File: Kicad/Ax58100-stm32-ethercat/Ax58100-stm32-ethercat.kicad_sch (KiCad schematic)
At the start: 0 parts

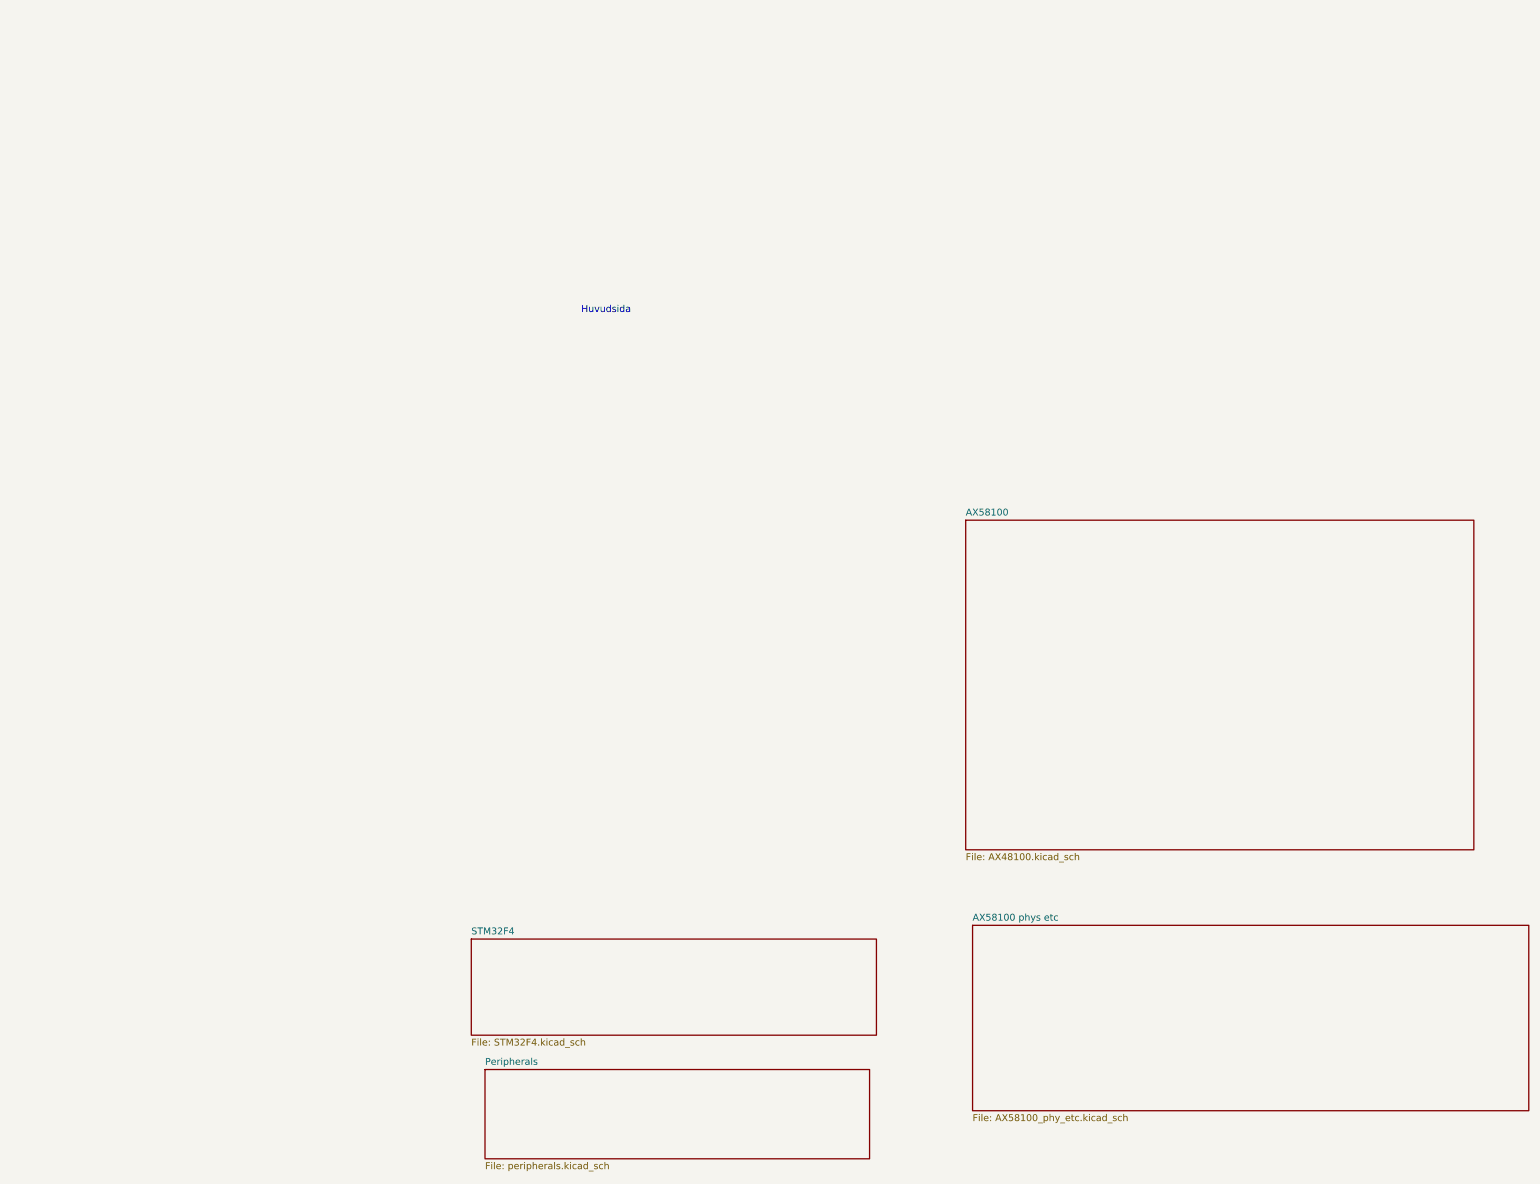
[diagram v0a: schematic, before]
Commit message: Steppers, encoders, IO, etc remapped
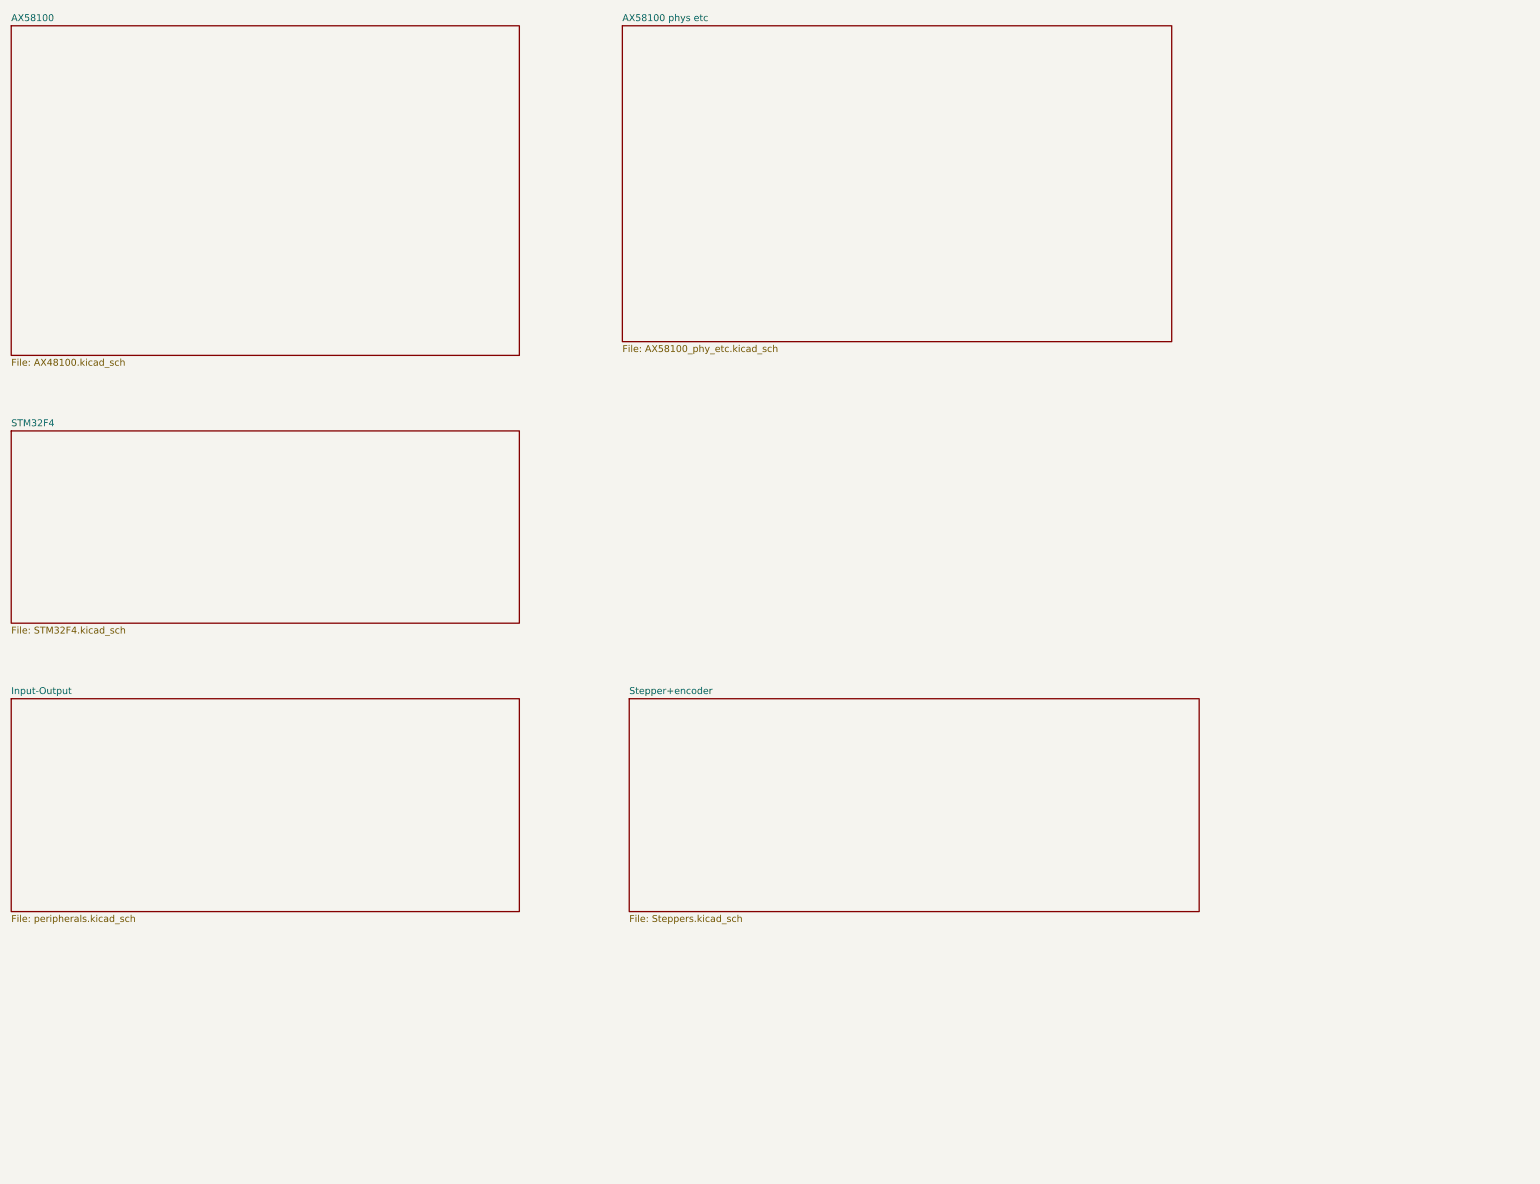
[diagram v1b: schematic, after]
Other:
- sheet Peripherals renamed Input-Output
- added sheet Stepper+encoder (Steppers.kicad_sch)
- note removed: "Huvudsida"
- title: (none) -> MetalMusings EaserCAT 3000
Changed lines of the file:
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@@
 (kicad_sch (version 20230121) (generator eeschema)
-  (paper "A3")
-  (text "Huvudsida" (at 162.56 85.09 0)
-    (effects (font (size 1.27 1.27)) (justify left bottom))
+  (paper "A4")
+  (title_block
+    (title "MetalMusings EaserCAT 3000")
   )
-  (sheet (at 144.78 224.79) (size 71.12 16.51) (fields_autoplaced)
+  (sheet (at 57.15 156.21) (size 93.98 39.37) (fields_autoplaced)
     (stroke (width 0.1524) (type solid))
     (fill (color 0 0 0 0.0000))
-    (property "Sheetname" "Peripherals" (at 144.78 224.0784 0)
+    (property "Sheetname" "Input-Output" (at 57.15 155.4984 0)
       (effects (font (size 1.27 1.27)) (justify left bottom))
     )
-    (property "Sheetfile" "peripherals.kicad_sch" (at 144.78 241.8846 0)
+    (property "Sheetfile" "peripherals.kicad_sch" (at 57.15 196.1646 0)
       (effects (font (size 1.27 1.27)) (justify left top))
     )
@@
     )
   )
-  (sheet (at 234.95 198.12) (size 102.87 34.29) (fields_autoplaced)
+  (sheet (at 170.18 31.75) (size 101.6 58.42) (fields_autoplaced)
     (stroke (width 0.1524) (type solid))
     (fill (color 0 0 0 0.0000))
-    (property "Sheetname" "AX58100 phys etc" (at 234.95 197.4084 0)
+    (property "Sheetname" "AX58100 phys etc" (at 170.18 31.0384 0)
       (effects (font (size 1.27 1.27)) (justify left bottom))
     )
-    (property "Sheetfile" "AX58100_phy_etc.kicad_sch" (at 234.95 232.9946 0)
+    (property "Sheetfile" "AX58100_phy_etc.kicad_sch" (at 170.18 90.7546 0)
       (effects (font (size 1.27 1.27)) (justify left top))
     )
@@
     )
   )
-  (sheet (at 233.68 123.19) (size 93.98 60.96) (fields_autoplaced)
+  (sheet (at 57.15 31.75) (size 93.98 60.96) (fields_autoplaced)
     (stroke (width 0.1524) (type solid))
     (fill (color 0 0 0 0.0000))
-    (property "Sheetname" "AX58100" (at 233.68 122.4784 0)
+    (property "Sheetname" "AX58100" (at 57.15 31.0384 0)
       (effects (font (size 1.27 1.27)) (justify left bottom))
     )
-    (property "Sheetfile" "AX48100.kicad_sch" (at 233.68 184.7346 0)
+    (property "Sheetfile" "AX48100.kicad_sch" (at 57.15 93.2946 0)
       (effects (font (size 1.27 1.27)) (justify left top))
     )
@@
     )
   )
-  (sheet (at 142.24 200.66) (size 74.93 17.78) (fields_autoplaced)
+  (sheet (at 171.45 156.21) (size 105.41 39.37) (fields_autoplaced)
     (stroke (width 0.1524) (type solid))
     (fill (color 0 0 0 0.0000))
-    (property "Sheetname" "STM32F4" (at 142.24 199.9484 0)
+    (property "Sheetname" "Stepper+encoder" (at 171.45 155.4984 0)
       (effects (font (size 1.27 1.27)) (justify left bottom))
     )
-    (property "Sheetfile" "STM32F4.kicad_sch" (at 142.24 219.0246 0)
+    (property "Sheetfile" "Steppers.kicad_sch" (at 171.45 196.1646 0)
       (effects (font (size 1.27 1.27)) (justify left top))
     )
+    (instances
+      (project "Ax58100-stm32-ethercat"
+        (path "/5597aedc-b607-407f-bbfd-31b3b298ecb1" (page "6"))
+      )
+    )
+  )
+  (sheet (at 57.15 106.68) (size 93.98 35.56) (fields_autoplaced)
+    (stroke (width 0.1524) (type solid))
+    (fill (color 0 0 0 0.0000))
+    (property "Sheetname" "STM32F4" (at 57.15 105.9684 0)
+      (effects (font (size 1.27 1.27)) (justify left bottom))
+    )
+    (property "Sheetfile" "STM32F4.kicad_sch" (at 57.15 142.8246 0)
+      (effects (font (size 1.27 1.27)) (justify left top))
+    )
